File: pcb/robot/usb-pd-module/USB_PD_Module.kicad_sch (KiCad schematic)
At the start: 58 parts, among them J4 USB4151-GF-C, J9 Conn_01x16, U1 TPS22950CDDCR, U11 MAX77958EWV+T, U15 TPD1E05U06, U17 TPS61253AYFFT, U19 TPD1E05U06, U20 TPD1E05U06, U21 TPD1E05U06, U22 TPD1E05U06, U23 TPD1E05U06, U24 TVS0500DRV

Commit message: Add selectable 0-ohm CC jumpers on USB-PD module (addresses #3)
Insert R3 (CC1, populated) and R4 (CC2, DNP) in series between J4 and
the MAX77958 CC1/CC2 pins, so only one CC path is active for a direct
male USB-C plug configuration. Both jumpers placed in a separate area
with clear access for rework/probing.

Also cleaned up ERC findings found while editing: no-connect markers
on unused TPS22950CDDCR pin 6 and Conn_01x16 pin 5, and reorganized
power netclasses (Power_Module -> power_1A / Default).
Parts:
- added R3, R4: 0, robot:R_0603_1608Metric, symbol Device:R
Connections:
- net at J4.B5 (CC2), TP4.1, U22.1 (I/O): now also R4.1; no longer C45.1, U11.A4 (CC2)
- net at J4.A5 (CC1), TP3.1, U23.1 (I/O): now also R3.1; no longer C46.1, U11.A3 (CC1)
- new net: C45.1, R4.2, U11.A4 (CC2)
- new net: C46.1, R3.2, U11.A3 (CC1)
- no-connect marks 11 -> 13
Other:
- note added: "NOTE: Only ONE of R96 (CC1) / R97 (CC2) should be populated for a direct male USB-C plug configuration. Default: R3 populated, R4 DNP. The unused CC-position contact must remain floating - do NOT tie it to 5V, GND, Rp, Rd, or the other CC line."
- moved on the sheet: C48, R75, TP3, TP4

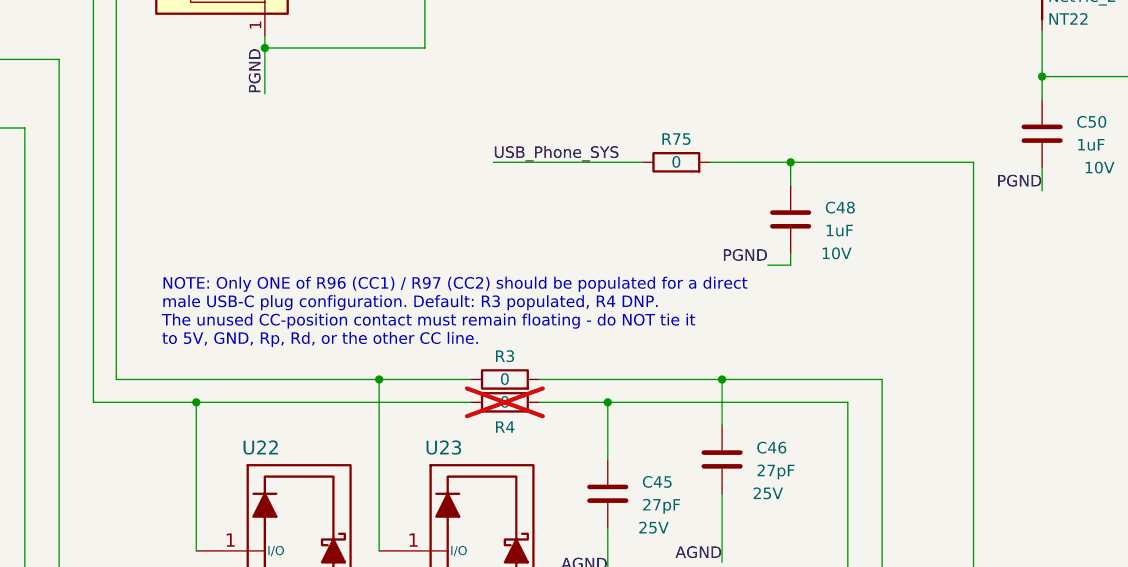
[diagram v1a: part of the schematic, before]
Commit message: Fix reversed motor connector pins on J3/J5 (fixes #15)
Swap pins 1/6 (motor phase polarity) and 2/5 (encoder VCC/GND) on
both motor JST connectors (J3, J5), so standard JST cables work
without custom re-pinning and without needing a software-side
forward/backward negation workaround. Pins 3/4 (encoder A/B) left
untouched. PCB copper re-routed to match; verified 0 unconnected
items via DRC and no new ERC violations on J3/J5.

Firmware's negation workaround should be removed once this hardware
revision is in use, or the two corrections will cancel out.

Fix leftover note typo and grid nudge (follow-up to #3)

Correct CC jumper note in USB_PD_Module.kicad_sch to reference the
actual R3/R4 designators used, and nudge SW1 onto grid in
Protection.kicad_sch. No net changes.
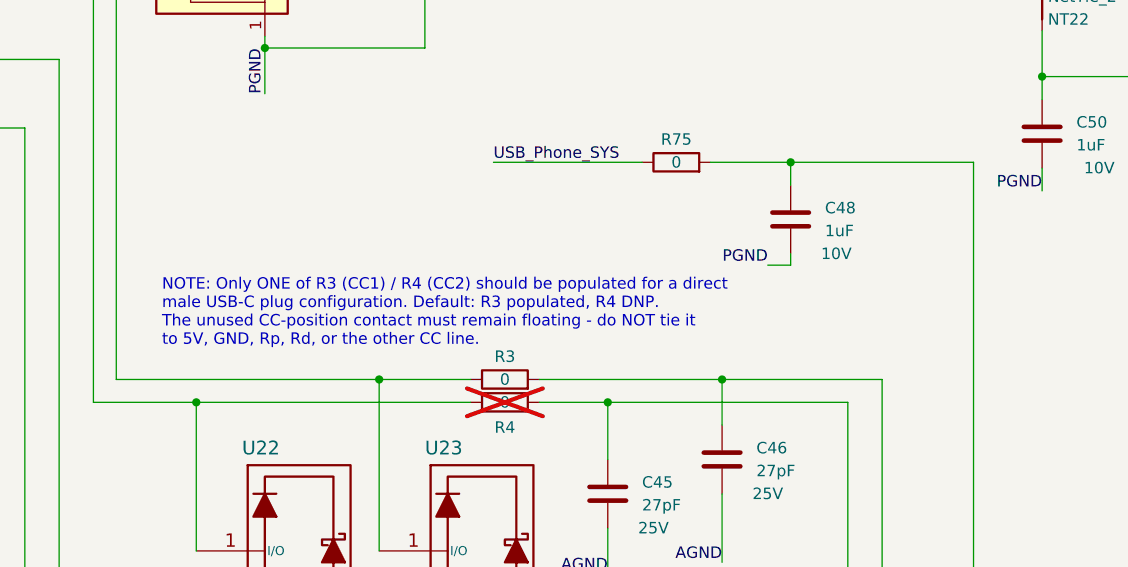
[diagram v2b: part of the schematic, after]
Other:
- note added: "NOTE: Only ONE of R3 (CC1) / R4 (CC2) should be populated for a direct male USB-C plug configuration. Default: R3 populated, R4 DNP. The unused CC-position contact must remain floating - do NOT tie it to 5V, GND, Rp, Rd, or the other CC line."
- note removed: "NOTE: Only ONE of R96 (CC1) / R97 (CC2) should be populated for a direct male USB-C plug configuration. Default: R3 populated, R4 DNP. The unused CC-position contact must remain floating - do NOT tie it to 5V, GND, Rp, Rd, or the other CC line."
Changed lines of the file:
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@@
 		)
 	)
-	(text "NOTE: Only ONE of R96 (CC1) / R97 (CC2) should be populated for a direct \nmale USB-C plug configuration. Default: R3 populated, R4 DNP. \nThe unused CC-position contact must remain floating - do NOT tie it \nto 5V, GND, Rp, Rd, or the other CC line."
+	(text "NOTE: Only ONE of R3 (CC1) / R4 (CC2) should be populated for a direct \nmale USB-C plug configuration. Default: R3 populated, R4 DNP. \nThe unused CC-position contact must remain floating - do NOT tie it \nto 5V, GND, Rp, Rd, or the other CC line."
 		(exclude_from_sim no)
 		(at 151.13 167.894 0)
